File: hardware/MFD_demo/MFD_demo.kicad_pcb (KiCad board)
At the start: 2 copper layers, 52 parts, among them J1 Pins_Ard, J2 POWER, Q1 IRF740, Q10 IRF740, Q2 IRF740, Q3 IRF740, Q4 IRF740, Q5 IRF740, Q6 IRF740, Q7 IRF740, Q8 IRF740, Q9 IRF740

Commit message: Update documents
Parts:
- moved R12 138.1 mm to (224.8, 110.7)
- moved R18 138.1 mm to (224.8, 105.6)
- moved R19 138.1 mm to (224.8, 89.4)
- moved R6 138.1 mm to (224.8, 95.3)
- moved R8 138.1 mm to (224.8, 82.9)
- moved R9 138.1 mm to (224.8, 100.4)
- moved D1 94.2 mm to (195.4, 153.6)
- moved D6 94.2 mm to (208.2, 140.5)
- moved Q8 94.2 mm to (197.9, 141.8)
- moved Q7 94.2 mm to (197.9, 135.8)
- moved D10 94.2 mm to (196.6, 147.1)
- moved D9 94.2 mm to (203.1, 147.1)
- moved D3 77.4 mm to (219.6, 62.5)
- moved D8 77.4 mm to (226.1, 62.5)
- moved J2 77.4 mm to (225.5, 54.7)
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
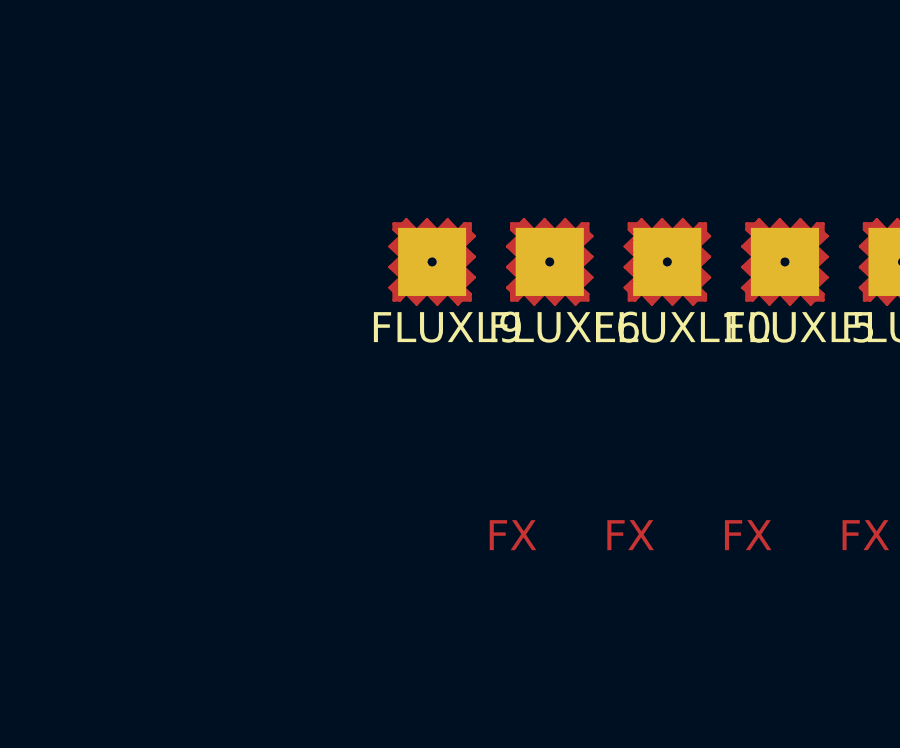
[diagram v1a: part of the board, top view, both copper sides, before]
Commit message: Modify folder structure
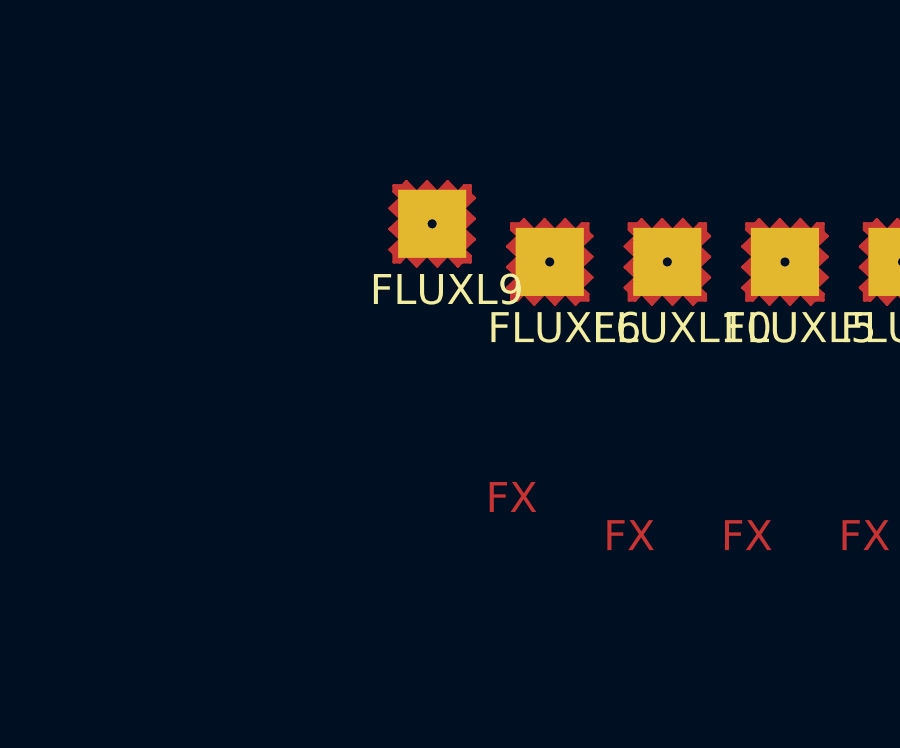
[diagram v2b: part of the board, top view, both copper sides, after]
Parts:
- moved FLUXL9 1.27 mm to (139.5, 110.2)
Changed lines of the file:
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@@
   )
   (footprint "GaudiLabsFootPrints:FLUXPAD_2_75_4MIL_FINAL" (layer "F.Cu")
-    (at 139.48 111.506)
+    (at 139.48 110.236)
     (property "Sheetfile" "MFD_demo.kicad_sch")
     (property "Sheetname" "")

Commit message: Update schem + layout PCB: Changes from 10 electrodes -> 6 electrodes
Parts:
- removed D10, D7, D8, D9: LED, LED_THT:LED_D4.0mm
- removed Q10, Q7, Q8, Q9: IRF740, Package_TO_SOT_THT:TO-220-3_Vertical
- removed R10, R16, R20, R5: R, Resistor_THT:R_Axial_DIN0207_L6.3mm_D2.5mm_P10.16mm_Horizontal
- removed R14, R15, R17, R18: 1K, Resistor_THT:R_Axial_DIN0207_L6.3mm_D2.5mm_P10.16mm_Horizontal
- D1, D2, D3, D4, D5, D6: footprint LED_THT:LED_D4.0mm -> LED_THT:LED_D5.0mm_IRBlack
- R1, R11, R12, R13, R19, R2, R3, R4, R6, R7, R8, R9: footprint Resistor_THT:R_Axial_DIN0207_L6.3mm_D2.5mm_P10.16mm_Horizontal -> Resistor_THT:R_Axial_DIN0204_L3.6mm_D1.6mm_P5.08mm_Horizontal
- moved R2 151.3 mm to (98.6, 78.6), turned to -90 degrees
- moved R1 141.4 mm to (100.7, 132.8), turned to 90 degrees
- moved R12 131.5 mm to (96.1, 83.7), turned to 90 degrees
- moved Q1 131.3 mm to (101.2, 121.5), turned to 180 degrees
- moved R3 129.1 mm to (113.6, 132.8), turned to 90 degrees
- moved D3 119.7 mm to (120.9, 130.2)
- moved D6 119.5 mm to (104.4, 81.1), turned to 180 degrees
- moved R7 118.8 mm to (129.2, 127.7), turned to -90 degrees
- moved R19 115.4 mm to (109.9, 78.8), turned to -90 degrees
- moved R6 113.4 mm to (116.1, 127.7), turned to -90 degrees
- moved D4 112.1 mm to (127.2, 81.4), turned to 180 degrees
- moved R8 110.1 mm to (126.7, 132.8), turned to 90 degrees
- moved R9 107.2 mm to (118.9, 83.9), turned to 90 degrees
- moved D1 103.2 mm to (94.9, 130.3)
- moved R4 98.2 mm to (103.2, 127.8), turned to -90 degrees
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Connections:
- J1 pad 10: /LED_10 -> /pin_10
- J1 pad 7: /LED_7 -> /pin_7
- J1 pad 8: /LED_8 -> /pin_8
- J1 pad 9: /LED_9 -> /pin_9
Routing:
- net Net-(D4-Pad2): track 0.00 -> 7.69 mm
- net Net-(D5-Pad2): track 0.00 -> 7.69 mm
- net Net-(D3-Pad2): track 0.00 -> 7.69 mm
- net Net-(D2-Pad2): track 0.00 -> 7.69 mm
- net Net-(D1-Pad2): track 0.00 -> 7.69 mm
- net Net-(D6-Pad2): track 0.00 -> 7.66 mm
- net /PAD_6: track 0.00 -> 7.09 mm
- net /PAD_1: track 0.00 -> 7.08 mm
- net /LED_1: track 0.00 -> 7.08 mm
- net /LED_6: track 0.00 -> 7.07 mm
- net /PAD_5: track 0.00 -> 7.03 mm
- net /PAD_4: track 0.00 -> 7.03 mm
- net /PAD_3: track 0.00 -> 7.03 mm
- net /PAD_2: track 0.00 -> 7.02 mm
- net /LED_5: track 0.00 -> 7.02 mm
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
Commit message: Update PCB layout version 01
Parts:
- added J10: GND, Connector_PinSocket_2.54mm:PinSocket_1x03_P2.54mm_Vertical, F.Cu at (80.5, 91.5)
- added J3: GND_Electrodes, Connector_PinSocket_2.54mm:PinSocket_1x01_P2.54mm_Vertical, F.Cu at (123.2, 105.7)
- added J4: Ard_1, Connector_PinSocket_2.54mm:PinSocket_1x01_P2.54mm_Vertical, F.Cu at (98.8, 129.1)
- added J5: Ard_2, Connector_PinSocket_2.54mm:PinSocket_1x01_P2.54mm_Vertical, F.Cu at (117.0, 129.1)
- added J6: Ard_3, Connector_PinSocket_2.54mm:PinSocket_1x01_P2.54mm_Vertical, F.Cu at (134.9, 127.8)
- added J7: Ard_4, Connector_PinSocket_2.54mm:PinSocket_1x01_P2.54mm_Vertical, F.Cu at (124.7, 82.6)
- added J8: Ard_5, Connector_PinSocket_2.54mm:PinSocket_1x01_P2.54mm_Vertical, F.Cu at (106.7, 82.5)
- added J9: Ard_6, Connector_PinSocket_2.54mm:PinSocket_1x01_P2.54mm_Vertical, F.Cu at (88.7, 82.5)
- J1: value Pins_Ard -> GND_Electrodes; footprint Connector_PinHeader_2.54mm:PinHeader_1x10_P2.54mm_Vertical -> Connector_PinSocket_2.54mm:PinSocket_1x01_P2.54mm_Vertical
- moved J2 81.4 mm to (80.5, 83.1)
- moved J1 36.0 mm to (100.5, 105.8), turned to 0 degrees
- moved D4 9.99 mm to (136.4, 77.5)
- moved R2 9.83 mm to (88.8, 78.0), turned to 0 degrees
- moved D1 8.58 mm to (86.7, 132.6)
- moved R9 8.45 mm to (127.3, 82.6), turned to 0 degrees
- moved R8 8.27 mm to (134.9, 133.0), turned to 180 degrees
- moved R4 7.10 mm to (96.2, 129.1), turned to 180 degrees
- moved Q6 6.78 mm to (91.3, 90.1)
- moved Q4 6.39 mm to (127.3, 90.4)
- moved D6 6.06 mm to (99.6, 77.5)
- moved FLUXL4 5.60 mm to (114.7, 104.4)
- moved FLUXL6 5.59 mm to (109.1, 104.4)
- moved Q3 5.19 mm to (132.4, 121.6)
- moved Q1 5.03 mm to (96.2, 121.6)
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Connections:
- FLUXL10 pad 1: /PAD_10 -> Net-(FLUXL9-Pad1)
- FLUXL7 pad 1: /PAD_7 -> Net-(FLUXL8-Pad1)
- FLUXL8 pad 1: /PAD_8 -> Net-(FLUXL8-Pad1)
- FLUXL9 pad 1: /PAD_9 -> Net-(FLUXL9-Pad1)
- J1 pad 1: /LED_1 -> Net-(FLUXL8-Pad1)
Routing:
- net GND: track 0.00 -> 247.8 mm
- net /+HV: track 0.00 -> 184.3 mm
- net /PAD_6: track 7.09 -> 37.6 mm
- net /PAD_4: track 7.03 -> 37.4 mm
- net /PAD_1: track 7.08 -> 36.6 mm
- net /PAD_3: track 7.03 -> 36.0 mm
- net /PAD_5: track 7.03 -> 26.3 mm
- net /PAD_2: track 7.02 -> 26.0 mm
- net Net-(FLUXL8-Pad1): track 0.00 -> 9.98 mm
- net Net-(FLUXL9-Pad1): track 0.00 -> 9.91 mm
- net Net-(D2-Pad2): track 7.69 -> 4.13 mm
- net /LED_4: track 7.02 -> 10.4 mm
- net Net-(D1-Pad2): track 7.69 -> 4.36 mm
- net /LED_5: track 7.02 -> 10.2 mm
- net /LED_2: track 7.02 -> 10.1 mm
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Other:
- board text added: "+"
- board text added: "19130152"
- board text added: "GND"

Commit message: Update PCB layout
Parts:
- R1, R11, R12, R13, R19, R2, R3, R4, R6, R7, R8, R9: footprint Resistor_THT:R_Axial_DIN0204_L3.6mm_D1.6mm_P5.08mm_Horizontal -> Resistor_THT:R_Axial_DIN0207_L6.3mm_D2.5mm_P10.16mm_Horizontal
- moved J2 10.9 mm to (69.7, 82.2)
- moved R8 8.79 mm to (143.7, 133.1)
- moved R2 8.62 mm to (80.2, 77.3)
- moved D3 8.05 mm to (131.1, 133.2), turned to 180 degrees
- moved D6 6.57 mm to (93.0, 77.0), turned to 0 degrees
- moved R19 5.28 mm to (101.6, 77.3)
- moved R3 5.03 mm to (122.0, 133.1)
- moved D2 4.16 mm to (109.3, 133.1), turned to 180 degrees
- moved J10 4.12 mm to (76.4, 91.3)
- moved J7 4.02 mm to (128.5, 83.7)
- moved R9 4.02 mm to (131.1, 83.7)
- moved Q4 3.88 mm to (131.1, 90.0)
- moved J4 3.87 mm to (95.4, 127.2)
- moved J6 3.87 mm to (138.7, 127.1)
- moved R4 3.82 mm to (92.9, 127.2)
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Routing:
- net GND: track 247.8 -> 302.0 mm
- net /+HV: track 184.3 -> 232.1 mm
- net /PAD_3: track 36.0 -> 41.8 mm
- net /PAD_1: track 36.6 -> 41.3 mm
- net /PAD_4: track 37.4 -> 40.9 mm
- net /PAD_6: track 37.6 -> 41.1 mm
- net Net-(D2-Pad2): track 4.13 -> 6.97 mm
- net Net-(D6-Pad2): track 5.35 -> 7.99 mm
- net Net-(D5-Pad2): track 5.56 -> 8.17 mm
- net Net-(D1-Pad2): track 4.36 -> 6.93 mm
- net /LED_2: track 10.1 -> 8.15 mm
- net /LED_1: track 10.1 -> 8.10 mm
- net /LED_5: track 10.2 -> 8.56 mm
- net Net-(D4-Pad2): track 5.71 -> 7.30 mm
- net Net-(D3-Pad2): track 5.54 -> 7.10 mm
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
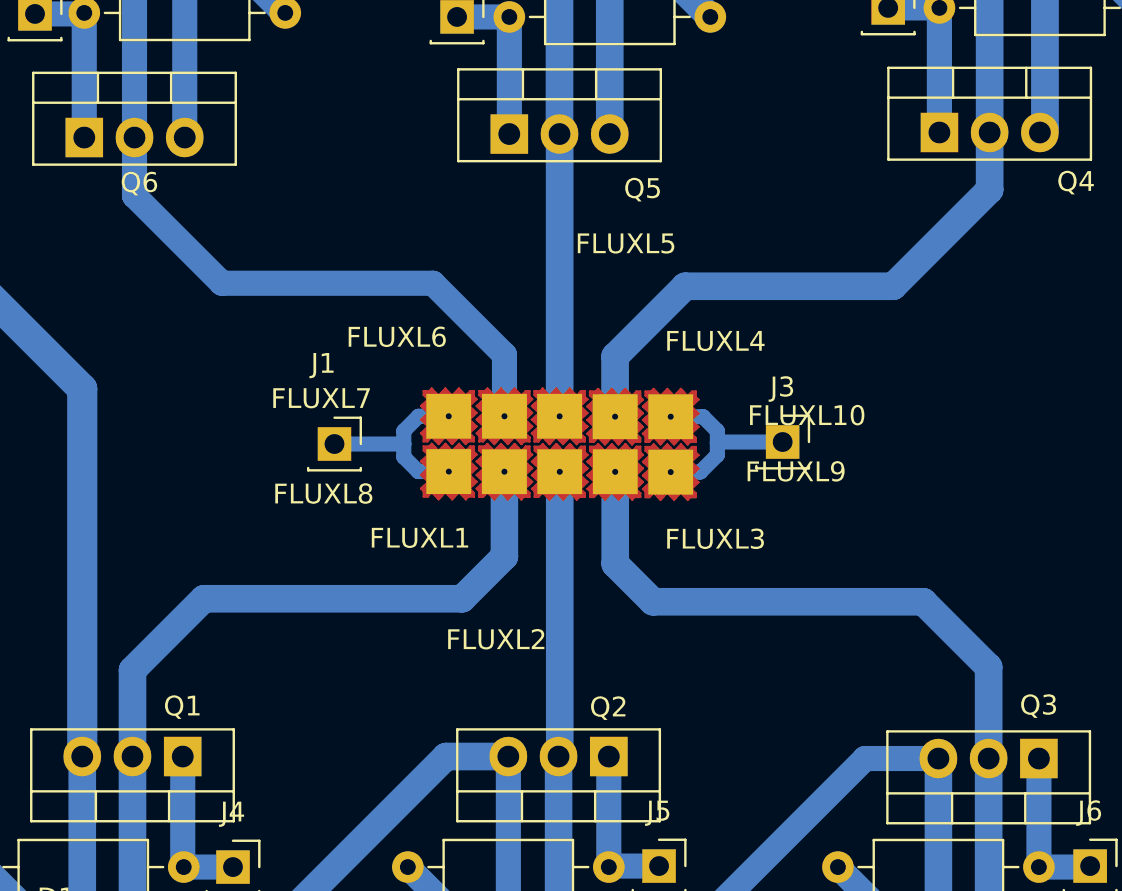
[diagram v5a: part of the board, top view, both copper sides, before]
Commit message: Update PCB layout: electrodes distances: 0.5mm
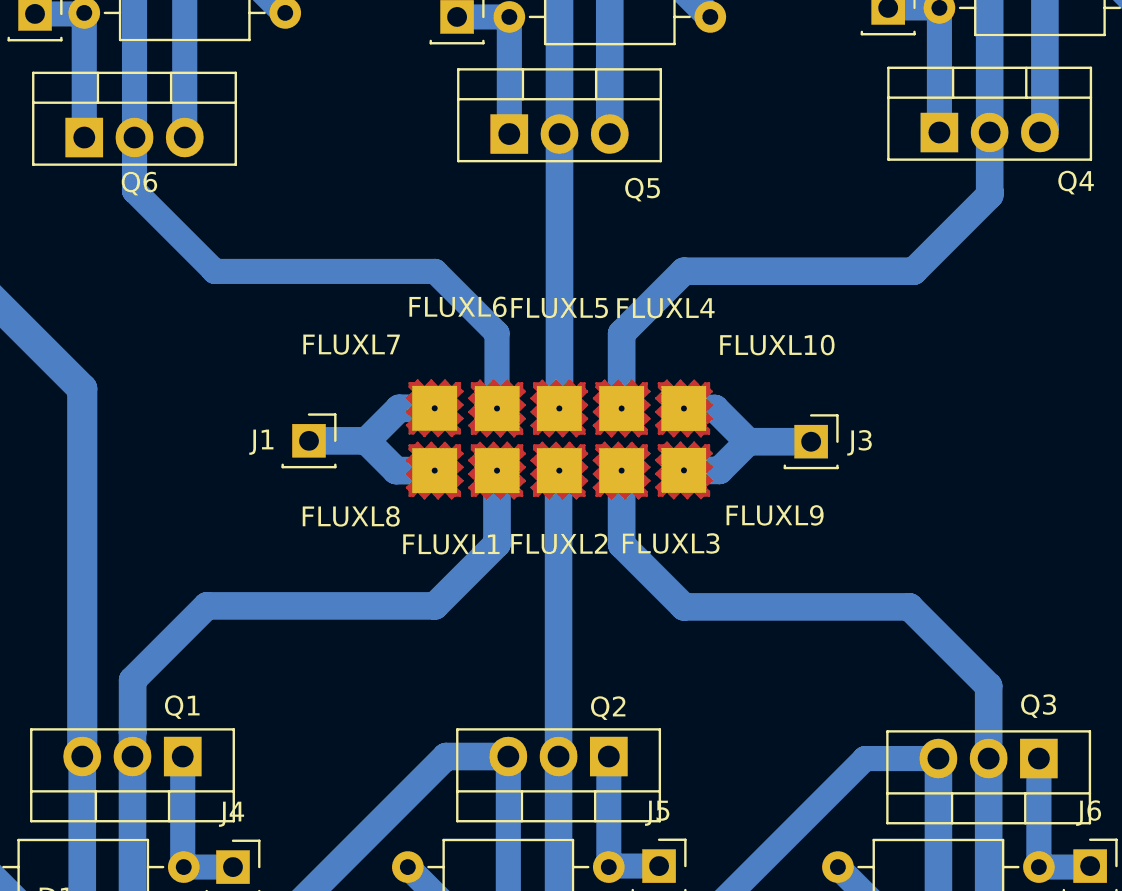
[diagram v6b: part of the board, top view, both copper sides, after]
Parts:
- moved J3 1.44 mm to (124.6, 105.7)
- moved J1 1.30 mm to (99.2, 105.6)
- moved FLUXL7 0.82 mm to (105.6, 104.0)
- moved FLUXL10 0.79 mm to (118.2, 104.0)
- moved FLUXL8 0.72 mm to (105.6, 107.1)
- moved FLUXL9 0.67 mm to (118.2, 107.1)
- moved FLUXL6 0.54 mm to (108.8, 104.0)
- moved FLUXL4 0.53 mm to (115.0, 104.0)
- moved FLUXL5 0.40 mm to (111.9, 104.0)
- moved FLUXL1 0.38 mm to (108.8, 107.1)
- moved FLUXL3 0.33 mm to (115.0, 107.1)
- moved FLUXL2 0.06 mm to (111.9, 107.1)
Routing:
- net /PAD_3: track 41.8 -> 40.4 mm
- net Net-(FLUXL7-Pad1): track 9.98 -> 11.1 mm
- net Net-(FLUXL10-Pad1): track 9.91 -> 11.0 mm
- net /PAD_1: track 41.3 -> 40.3 mm
